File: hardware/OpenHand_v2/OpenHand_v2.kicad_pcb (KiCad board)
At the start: 4 copper layers, 100 x 50 mm, 172 parts, among them J1 CONN_MOTOR_1, J10 CONN_FDBK_2, J11 CONN_EMG_2, J12 CONN_SWD, J13 CONN_POS_3, J2 CONN_MOTOR_2, J3 CONN_BATT, J4 CONN_POS_1, J5 CONN_USB_C, J6 CONN_MOTOR_3, J7 CONN_FDBK_1, J8 CONN_EMG_1, J9 CONN_POS_2, Q1 AO3401A, SW1 BTN_RST, SW2 SW_Push, U1 STM32F103RETx, U10 DRV8833PWP, U2 TPS565201DDCR, U3 AMS1117-3.3, U4 ICL7660, U5 LM324, U6 LM324, U7 DRV8833PWP, U8 DRV8833PWP, U9 DRV8833PWP, Y1 16MHz

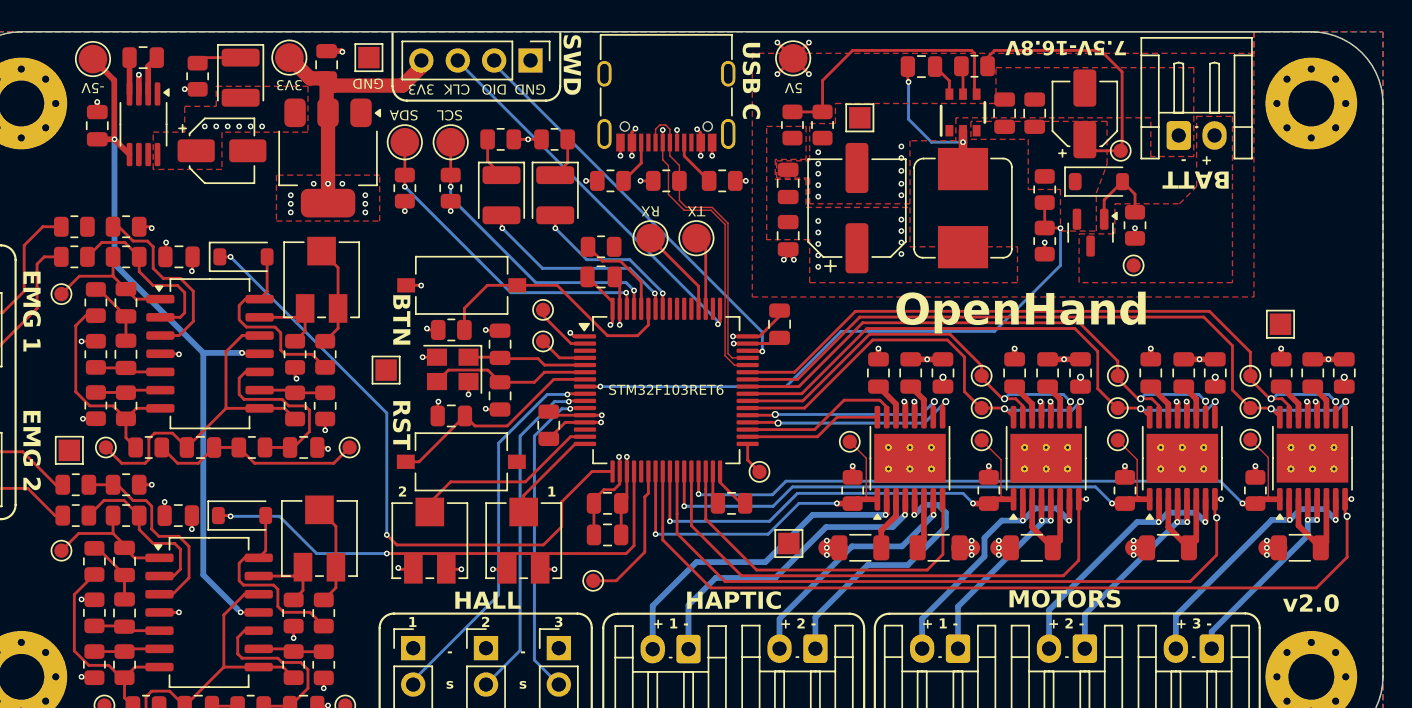
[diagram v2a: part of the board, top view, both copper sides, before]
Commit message: Finish OpenHand v2.0 board and prepare for ordering
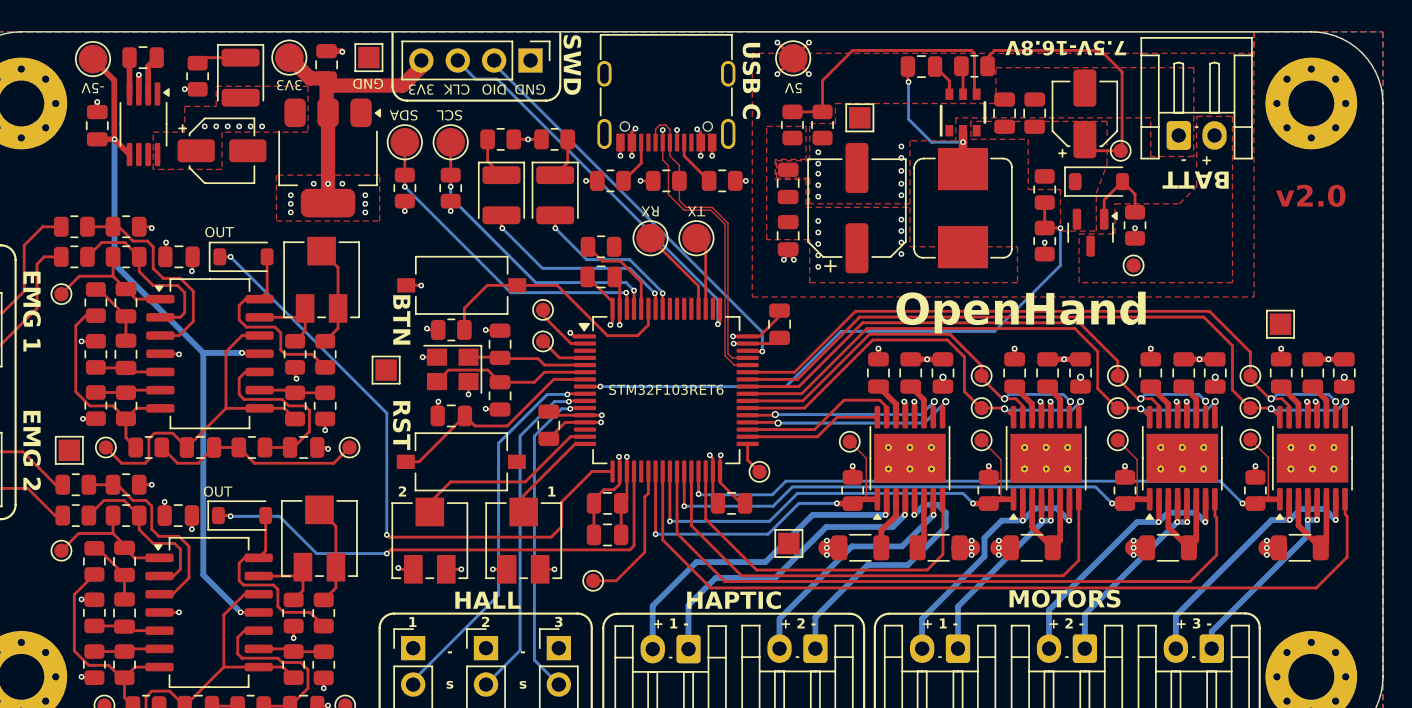
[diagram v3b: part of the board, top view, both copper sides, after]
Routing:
- net Net-(U5A-+): track 13.2 -> 14.9 mm
- net GND: track 67.0 -> 68.2 mm, vias 76 -> 77
- net +3V3: track 47.0 -> 48.2 mm, vias 20 -> 21
- net SWCLK: track 26.7 -> 27.5 mm
- net MOTOR_01_FAULT: track 37.5 -> 37.0 mm, vias 1 -> 0
- net MOTOR_03_FAULT: track 59.4 -> 58.9 mm, vias 2 -> 0
- net MOTOR_02_FAULT: track 48.5 -> 48.1 mm, vias 2 -> 0
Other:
- board text added: "JLCJLCJLCJLC"
- board text added: "OUT"
- board text added: "github.com/AleksaHeler/ProstheticHand"
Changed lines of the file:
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@@
 			)
 		)
+		(property ki_fp_filters "Connector*:*_1x??_*")
+		(sheetname "Root")
+		(sheetfile "OpenHand_v2.kicad_sch")
 		(attr through_hole)
 		(fp_line
@@
 			)
 		)
+		(property ki_fp_filters "Connector*:*_1x??_*")
+		(sheetname "Root")
+		(sheetfile "OpenHand_v2.kicad_sch")
 		(attr through_hole)
 		(fp_line
@@
 			)
 		)
+		(property ki_fp_filters "Connector*:*_1x??_*")
+		(sheetname "Root")
+		(sheetfile "OpenHand_v2.kicad_sch")
 		(attr through_hole)
 		(fp_line
@@
 			)
 		)
+		(property ki_fp_filters "Connector*:*_1x??_*")
+		(sheetname "Root")
+		(sheetfile "OpenHand_v2.kicad_sch")
 		(attr through_hole)
 		(fp_line
@@
 			)
 		)
+		(property ki_fp_filters "Connector*:*_1x??_*")
+		(sheetname "Root")
+		(sheetfile "OpenHand_v2.kicad_sch")
 		(attr through_hole)
 		(fp_line
@@
 			)
 		)
+		(property ki_fp_filters "Connector*:*_1x??_*")
+		(sheetname "Root")
+		(sheetfile "OpenHand_v2.kicad_sch")
 		(attr through_hole)
 		(fp_line
@@
 		(layer "Edge.Cuts")
 	)
+	(gr_text "v2.0"
+		(at 195 111.5 0)
+		(layer "F.Cu")
+		(effects
+			(font
+				(size 1.5 1.5)
+				(thickness 0.3)
+				(bold yes)
+			)
+		)
+	)
+	(gr_text "JLCJLCJLCJLC"
+		(at 149.9 104.9 -0)
+		(layer "B.SilkS")
+		(effects
+			(font
+				(size 1 1)
+				(thickness 0.15)
+			)
+			(justify mirror)
+		)
+	)
+	(gr_text "github.com/AleksaHeler/ProstheticHand"
+		(at 169 146.9 0)
+		(layer "B.SilkS")
+		(effects
+			(font
+				(size 1.2 1.2)
+				(thickness 0.22)
+				(bold yes)
+			)
+			(justify mirror)
+		)
+	)
 	(gr_text "HAPTIC"
 		(at 154.7 139.7 0)
@@
 		)
 	)
+	(gr_text "OUT"
+		(at 118.7 132.1 0)
+		(layer "F.SilkS")
+		(effects
+			(font
+				(size 0.7 0.7)
+				(thickness 0.15)
+			)
+		)
+	)
 	(gr_text "-5V"
 		(at 110 103.9 180)
@@
 		)
 	)
-	(gr_text "v2.0"
-		(at 195 139.9 0)
+	(gr_text "OUT"
+		(at 118.8 114 0)
 		(layer "F.SilkS")
 		(effects
 			(font
-				(size 1.2 1.2)
-				(thickness 0.22)
-				(bold yes)
+				(size 0.7 0.7)
+				(thickness 0.15)
 			)
 		)
@@
 	)
 	(segment
+		(start 109.6125 113.6)
+		(end 111.4 113.6)
+		(width 0.2)
+		(layer "F.Cu")
+		(net 25)
+	)
+	(segment
 		(start 116.1 117.2)
 		(end 117 118.1)
@@
 	)
 	(segment
+		(start 153.25 129.755)
+		(end 153.035 129.54)
+		(width 0.2)
+		(layer "F.Cu")
+		(net 26)
+	)
+	(segment
 		(start 146.75 119.325)
 		(end 146.75 120.45)
@@
 	)
 	(segment
+		(start 153.25 130.675)
+		(end 153.25 129.755)
+		(width 0.2)
+		(layer "F.Cu")
+		(net 26)
+	)
+	(segment
 		(start 137.449999 126.349999)
 		(end 137.4 126.3)
@@
 	)
 	(via
+		(at 153.035 129.54)
+		(size 0.4)
+		(drill 0.2)
+		(layers "F.Cu" "B.Cu")
+		(net 26)
+	)
+	(via
 		(at 109.3 127)
 		(size 0.4)
@@
 		(drill 0.2)
 		(layers "F.Cu" "B.Cu")
-		(locked yes)
 		(net 44)
 	)
@@
 	)
 	(segment
+		(start 153.749999 130.675)
+		(end 153.749999 129.587001)
+		(width 0.2)
+		(layer "F.Cu")
+		(net 79)
+	)
+	(segment
 		(start 146.250001 120.299999)
 		(end 146.250001 119.325)
@@
 	)
 	(segment
+		(start 153.749999 129.587001)
+		(end 153.797 129.54)
+		(width 0.2)
+		(layer "F.Cu")
+		(net 79)
+	)
+	(segment
 		(start 125.15 103.25)
 		(end 123.7 101.8)
@@
 	)
 	(via
+		(at 153.797 129.54)
+		(size 0.4)
+		(drill 0.2)
+		(layers "F.Cu" "B.Cu")
+		(net 79)
+	)
+	(via
 		(at 129 112)
 		(size 0.4)
@@
 	(segment
 		(start 130.5 136.4)
-		(end 147.2 136.4)
+		(end 130.756 136.144)
+		(width 0.2)
+		(layer "F.Cu")
+		(net 95)
+	)
+	(segment
+		(start 130.756 136.144)
+		(end 147.456 136.144)
+		(width 0.2)
+		(layer "F.Cu")
+		(net 95)
+	)
+	(segment
+		(start 147.456 136.144)
+		(end 147.75 135.85)
 		(width 0.2)
 		(layer "F.Cu")
@@
 		(net 95)
 	)
-	(segment
-		(start 147.2 136.4)
-		(end 147.75 135.85)
-		(width 0.2)
-		(layer "F.Cu")
-		(net 95)
-	)
 	(via
 		(at 130.5 136.4)
@@
 	)
 	(segment
-		(start 142.7 132.8)
-		(end 144.825 130.675)
+		(start 142.7 134.525)
+		(end 142.7 132.8)
 		(width 0.2)
 		(layer "F.Cu")
@@
 	)
 	(segment
-		(start 131.2 135.8)
-		(end 141.425 135.8)
+		(start 130.655 135.255)
+		(end 141.97 135.255)
 		(width 0.2)
 		(layer "F.Cu")
@@
 	)
 	(segment
-		(start 142.7 134.525)
-		(end 142.7 132.8)
+		(start 130.5 135.1)
+		(end 130.655 135.255)
 		(width 0.2)
 		(layer "F.Cu")
@@
 	)
 	(segment
-		(start 144.825 130.675)
-		(end 146.250001 130.675)
+		(start 142.7 132.8)
+		(end 144.825 130.675)
 		(width 0.2)
 		(layer "F.Cu")
@@
 	)
 	(segment
-		(start 130.5 135.1)
-		(end 131.2 135.8)
+		(start 141.97 135.255)
+		(end 142.7 134.525)
 		(width 0.2)
 		(layer "F.Cu")
@@
 	)
 	(segment
-		(start 141.425 135.8)
-		(end 142.7 134.525)
+		(start 144.825 130.675)
+		(end 146.250001 130.675)
 		(width 0.2)
 		(layer "F.Cu")
@@
 	)
 	(segment
-		(start 178.775 132.6125)
-		(end 179.2875 132.6125)
-		(width 0.2)
-		(layer "F.Cu")
-		(net 101)
-	)
-	(segment
 		(start 155.25 137.95)
 		(end 177.7 137.95)
@@
 	)
 	(segment
-		(start 179.2875 132.6125)
-		(end 179.3 132.6)
-		(width 0.2)
-		(layer "F.Cu")
-		(net 101)
-	)
-	(via
-		(at 179.3 132.6)
-		(size 0.4)
-		(drill 0.2)
-		(layers "F.Cu" "B.Cu")
-		(net 101)
-	)
-	(segment
-		(start 188.275 132.6125)
-		(end 188.6875 132.6125)
-		(width 0.2)
-		(layer "F.Cu")
-		(net 102)
-	)
-	(segment
 		(start 188.4 136.5)
 		(end 188.4 133.9)
@@
 	)
 	(segment
-		(start 188.6875 132.6125)
-		(end 188.7 132.6)
-		(width 0.2)
-		(layer "F.Cu")
-		(net 102)
-	)
-	(segment
 		(start 186.55 138.35)
 		(end 188.4 136.5)
@@
 		(net 102)
 	)
-	(via
-		(at 188.7 132.6)
-		(size 0.4)
-		(drill 0.2)
-		(layers "F.Cu" "B.Cu")
-		(net 102)
-	)
-	(via
-		(at 188.4 133.9)
-		(size 0.5)
-		(drill 0.3)
-		(layers "F.Cu" "B.Cu")
-		(net 102)
-	)
 	(segment
 		(start 164.4 121.5)
@@
 	)
 	(segment
-		(start 197.7875 132.6125)
-		(end 197.8 132.6)
-		(width 0.2)
-		(layer "F.Cu")
-		(net 107)
-	)
-	(segment
-		(start 197.355 132.6125)
-		(end 197.7875 132.6125)
-		(width 0.2)
-		(layer "F.Cu")
-		(net 107)
-	)
-	(segment
 		(start 149.75 135.45)
 		(end 153.1 138.8)
@@
 		(net 107)
 	)
-	(via
-		(at 197.8 132.6)
-		(size 0.4)
-		(drill 0.2)
-		(layers "F.Cu" "B.Cu")
-		(net 107)
-	)
-	(via
-		(at 197.5 133.8)
-		(size 0.5)
-		(drill 0.3)
-		(layers "F.Cu" "B.Cu")
-		(net 107)
-	)
 	(segment
 		(start 152.75 131.9)
@@
 	)
 	(segment
-		(start 153.6 120.2)
-		(end 135.7 102.3)
+		(start 153.6 118.7)
+		(end 138.2 103.3)
 		(width 0.2)
 		(layer "B.Cu")
@@
 	(segment
 		(start 153.6 120.4)
-		(end 153.6 120.2)
+		(end 153.6 118.7)
+		(width 0.2)
+		(layer "B.Cu")
+		(net 127)
+	)
+	(segment
+		(start 138.2 103.3)
+		(end 136.7 103.3)
+		(width 0.2)
+		(layer "B.Cu")
+		(net 127)
+	)
+	(segment
+		(start 136.7 103.3)
+		(end 135.7 102.3)
 		(width 0.2)
 		(layer "B.Cu")
@@
 		(filled_areas_thickness no)
 		(keepout
-			(tracks not_allowed)
-			(vias not_allowed)
-			(pads not_allowed)
+			(tracks allowed)
+			(vias allowed)
+			(pads allowed)
 			(copperpour not_allowed)
 			(footprints allowed)

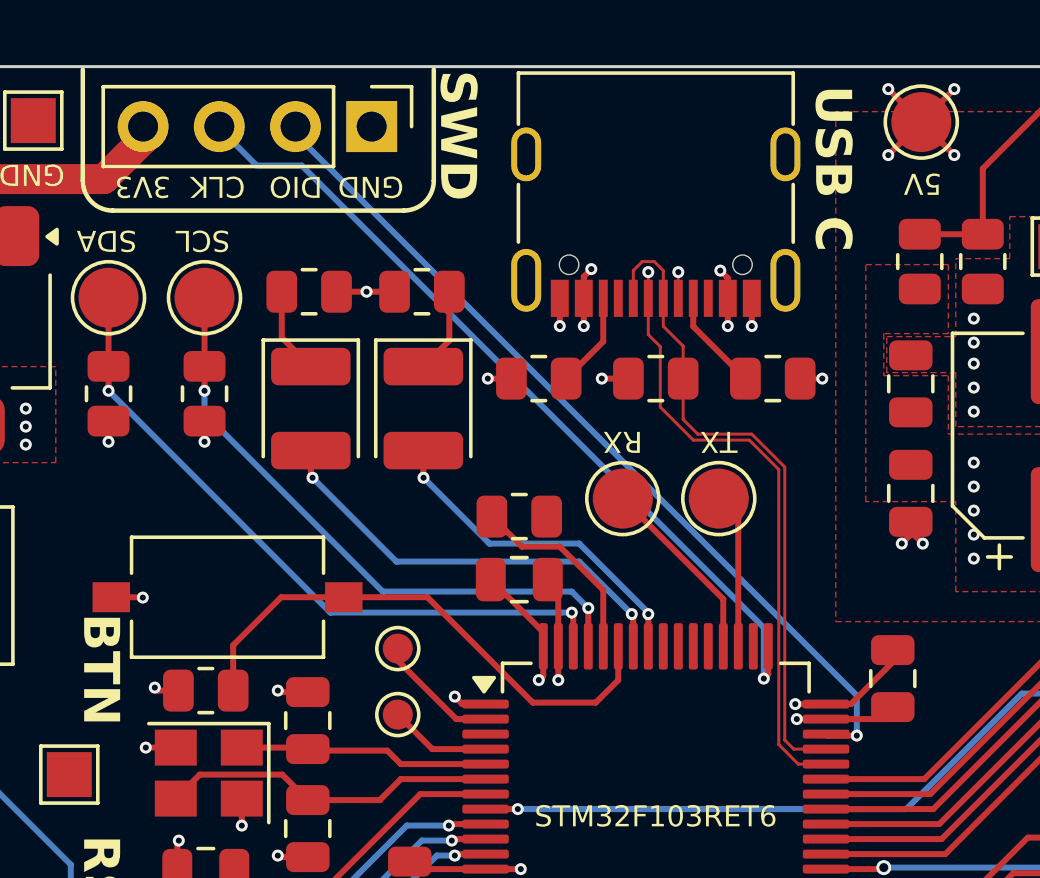
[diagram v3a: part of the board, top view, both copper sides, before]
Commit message: Update PCB and order from JLCPCB
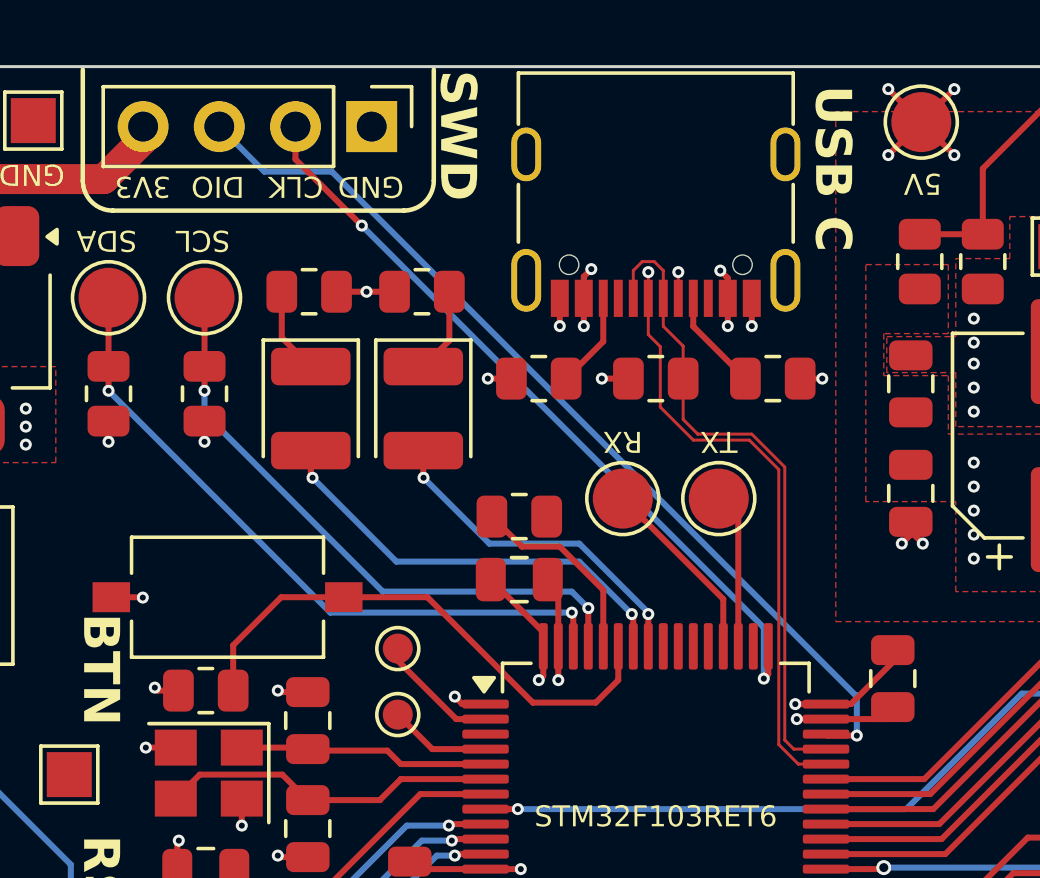
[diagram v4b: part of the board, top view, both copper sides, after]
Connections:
- J12 pad 2: SWDIO -> SWCLK
- J12 pad 3: SWCLK -> SWDIO
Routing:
- net SWDIO: track 28.8 -> 31.5 mm
- net SWCLK: track 27.5 -> 26.0 mm, vias 1 -> 2
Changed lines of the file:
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@@
 			(layers "*.Cu" "*.Mask")
 			(remove_unused_layers no)
-			(net 128 "SWDIO")
+			(net 127 "SWCLK")
 			(pinfunction "Pin_2")
 			(pintype "passive")
@@
 			(layers "*.Cu" "*.Mask")
 			(remove_unused_layers no)
-			(net 127 "SWCLK")
+			(net 128 "SWDIO")
 			(pinfunction "Pin_3")
 			(pintype "passive")
@@
 		)
 	)
-	(gr_text "CLK"
+	(gr_text "DIO"
 		(at 135.4 104 180)
 		(layer "F.SilkS")
@@
 		)
 	)
-	(gr_text "DIO"
+	(gr_text "CLK"
 		(at 138 104 180)
 		(layer "F.SilkS")
@@
 	)
 	(segment
+		(start 137.99 103.09)
+		(end 137.99 102)
+		(width 0.2)
+		(layer "F.Cu")
+		(net 127)
+	)
+	(segment
 		(start 153.749999 119.325)
 		(end 153.749999 120.250001)
@@
 		(net 127)
 	)
+	(segment
+		(start 140.2 105.3)
+		(end 137.99 103.09)
+		(width 0.2)
+		(layer "F.Cu")
+		(net 127)
+	)
 	(via
-		(at 153.6 120.4)
+		(at 140.2 105.3)
 		(size 0.4)
 		(drill 0.2)
@@
 		(net 127)
 	)
-	(segment
-		(start 153.6 118.7)
-		(end 138.2 103.3)
-		(width 0.2)
-		(layer "B.Cu")
+	(via
+		(at 153.6 120.4)
+		(size 0.4)
+		(drill 0.2)
+		(layers "F.Cu" "B.Cu")
 		(net 127)
 	)
@@
 	)
 	(segment
-		(start 138.2 103.3)
-		(end 136.7 103.3)
-		(width 0.2)
-		(layer "B.Cu")
-		(net 127)
-	)
-	(segment
-		(start 136.7 103.3)
-		(end 135.7 102.3)
+		(start 153.6 118.7)
+		(end 140.2 105.3)
 		(width 0.2)
 		(layer "B.Cu")
@@
 	)
 	(segment
+		(start 156.66 120.96)
+		(end 139.2 103.5)
+		(width 0.2)
+		(layer "B.Cu")
+		(net 128)
+	)
+	(segment
 		(start 156.7 122.3)
 		(end 156.7 120.96)
@@
 	)
 	(segment
+		(start 136.95 103.5)
+		(end 135.45 102)
+		(width 0.2)
+		(layer "B.Cu")
+		(net 128)
+	)
+	(segment
+		(start 139.2 103.5)
+		(end 136.95 103.5)
+		(width 0.2)
+		(layer "B.Cu")
+		(net 128)
+	)
+	(segment
 		(start 156.7 120.96)
-		(end 138.04 102.3)
+		(end 156.66 120.96)
 		(width 0.2)
 		(layer "B.Cu")

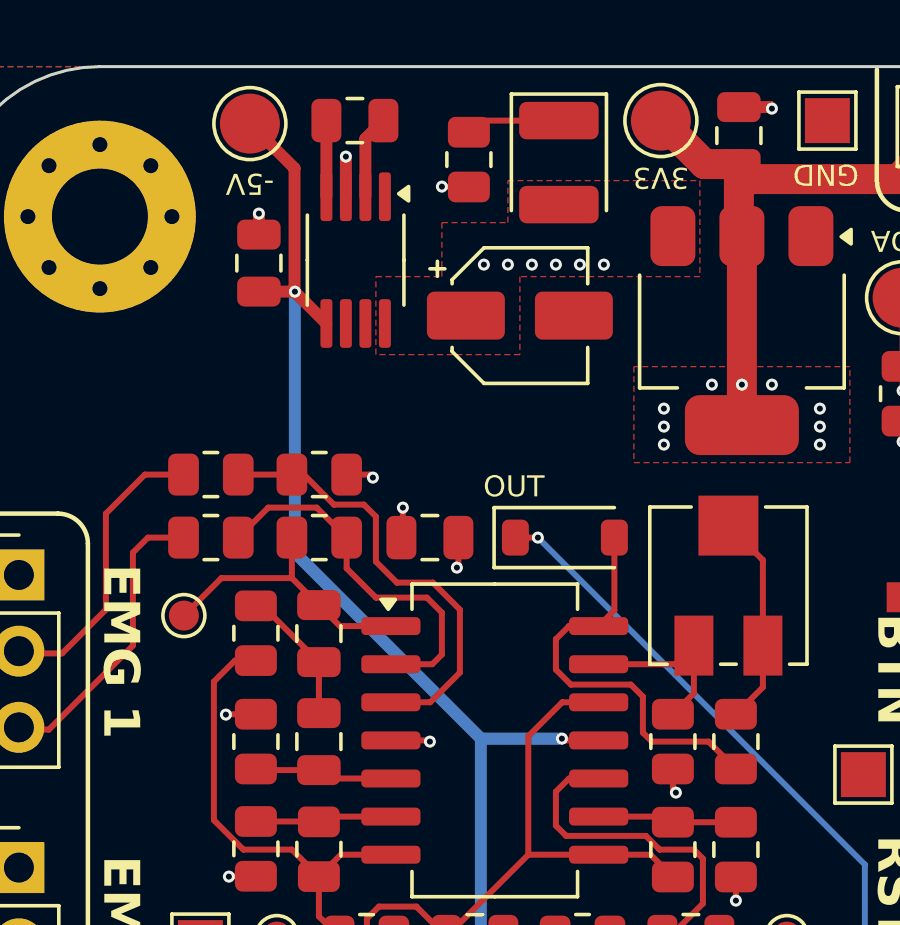
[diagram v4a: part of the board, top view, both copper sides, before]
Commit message: EMG sensor quickfix, upadte ADC and DMA config
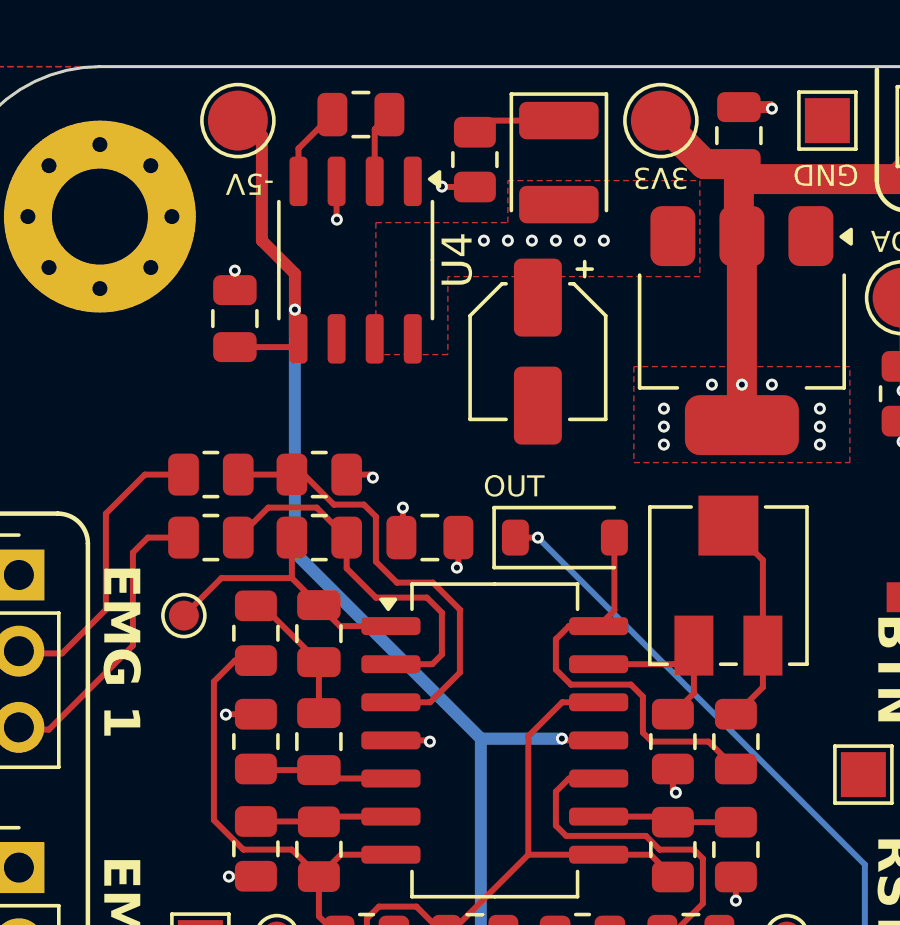
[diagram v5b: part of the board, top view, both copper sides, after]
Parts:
- C27, C28: value 470n -> 330n
- R8: value 4k7 -> 10k
- U4: footprint Package_SO:MSOP-8_3x3mm_P0.65mm -> Package_SO:SOP-8_3.9x4.9mm_P1.27mm
- U5, U6: value LM324 -> TL084
- moved C17 2.02 mm to (109.5, 108.4)
- moved C19 1.34 mm to (119.6, 109.5), turned to -90 degrees
- moved TP18 0.41 mm to (109.6, 101.8)
- moved C20 0.28 mm to (113.7, 101.6)
- moved R15 0.20 mm to (117.5, 103.1)
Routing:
- net -5V: track 50.5 -> 51.1 mm
